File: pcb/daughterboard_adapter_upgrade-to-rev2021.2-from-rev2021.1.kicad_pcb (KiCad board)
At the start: 2 copper layers, 20.2 x 52.2 mm, 4 parts, among them U1 MiniF4, U2 SN74LVC1T45DBV, U3 MiniF4

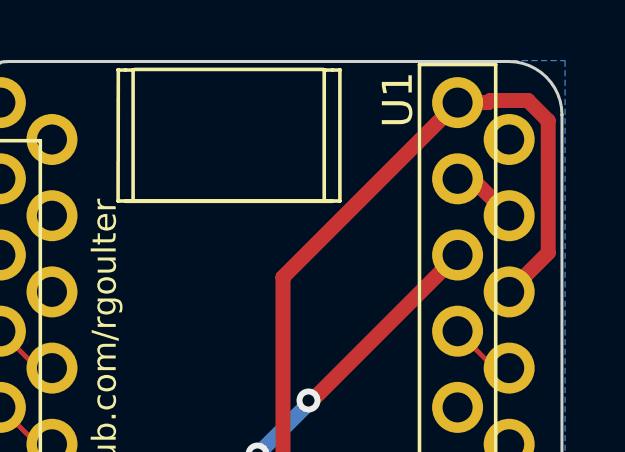
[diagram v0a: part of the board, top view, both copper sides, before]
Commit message: Kicad: Use "5V", "GND", "3V3" in symbol and footprint; update Sch+PCBs
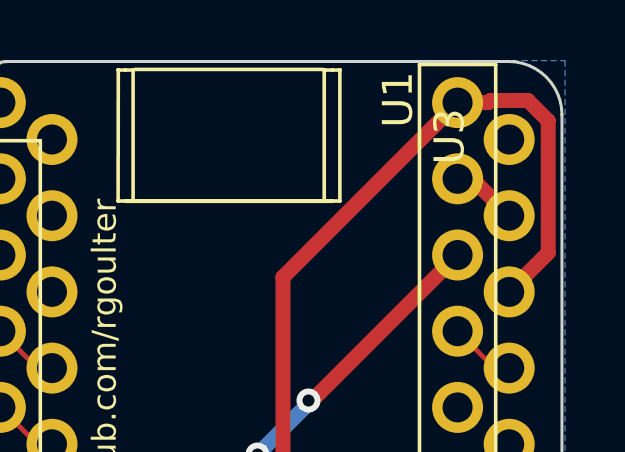
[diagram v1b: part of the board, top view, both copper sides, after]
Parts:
- U1, U3: footprint ProjectLocal:WeAct_MiniF4 -> ProjectLocal:WeAct_MiniF4_Staggerable_rev2020.1

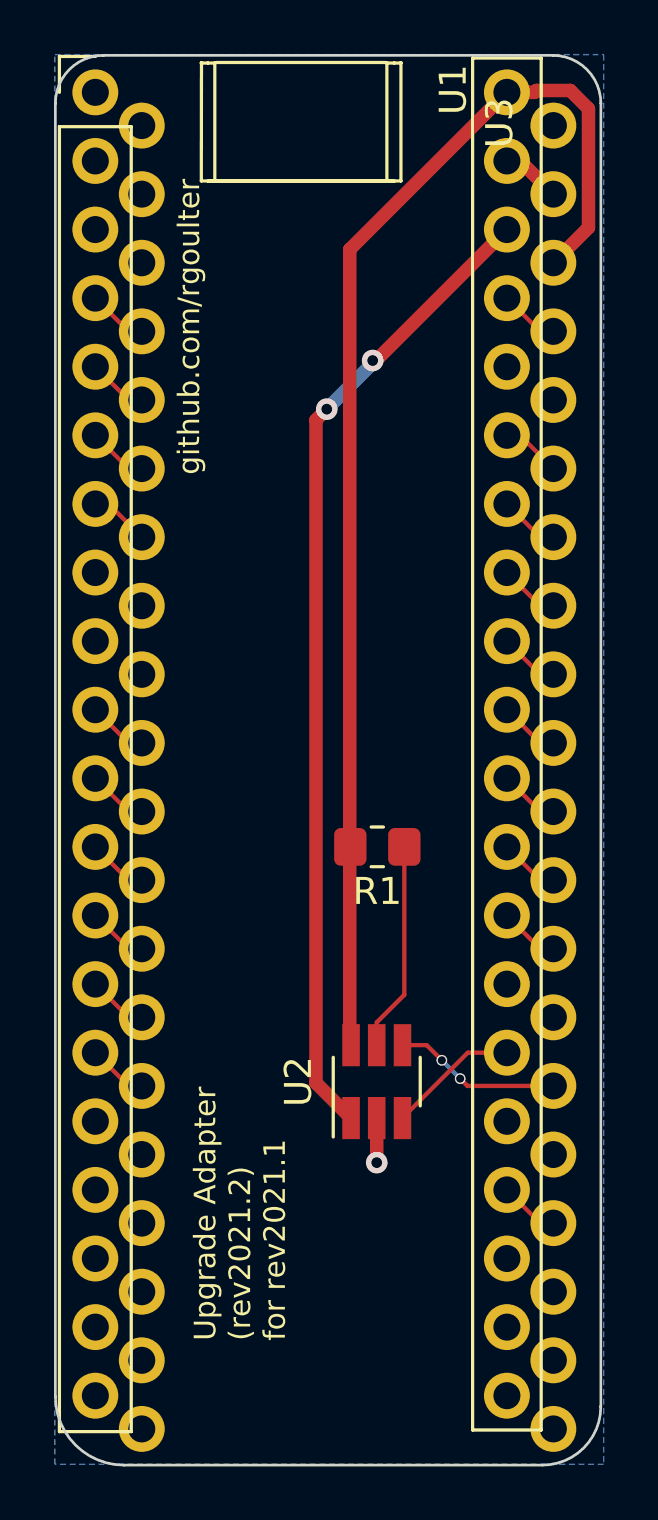
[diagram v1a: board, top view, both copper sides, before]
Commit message: Kicad: plot daughterboards
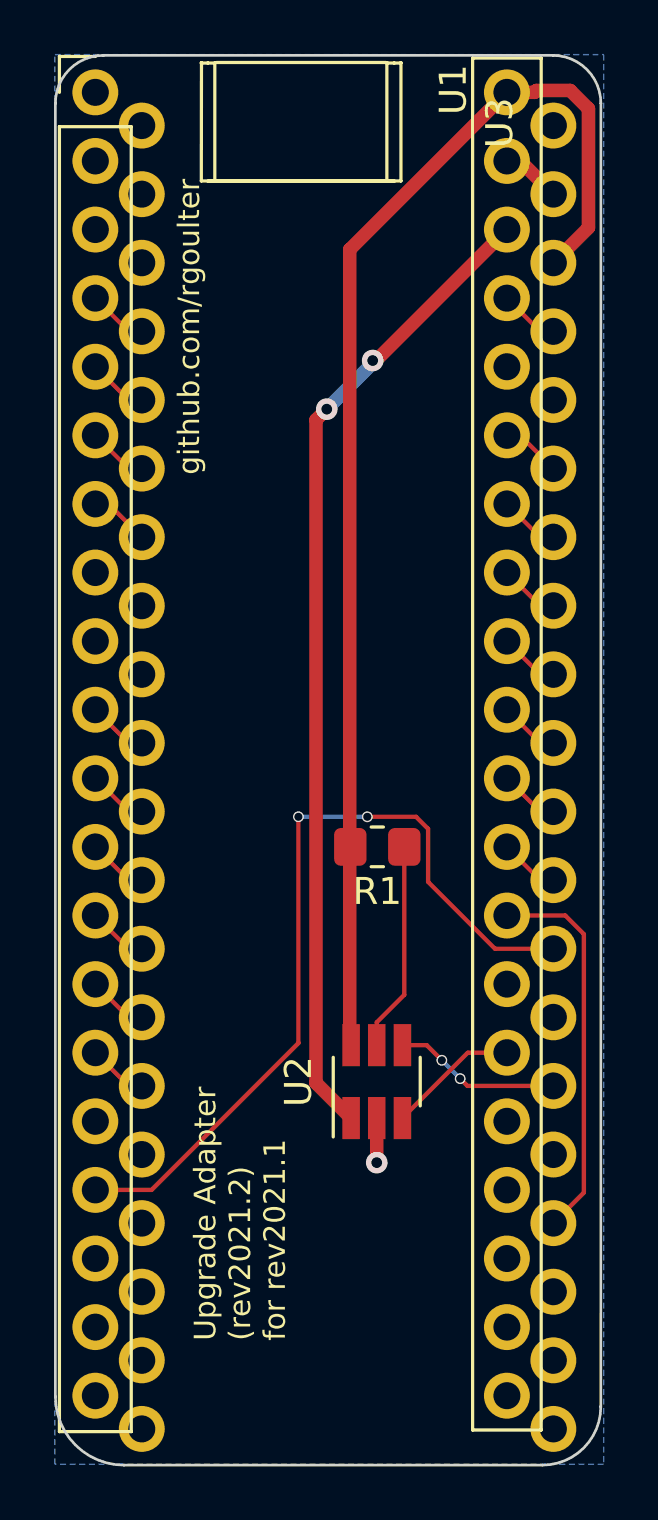
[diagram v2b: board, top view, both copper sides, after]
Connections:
- U1 pad 12: /SW31 -> /SW15
- U1 pad 4: /SW15 -> (no net)
- U1 pad 46: (no net) -> /SW31
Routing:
- net /SW31: track 2.23 -> 31.3 mm, vias 0 -> 2
- net /SW15: track 2.23 -> 14.8 mm
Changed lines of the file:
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@@
     (thickness 1.6)
     (drawings 14)
-    (tracks 74)
+    (tracks 87)
     (zones 0)
     (modules 4)
@@
       (outputformat 1)
       (mirror false)
-      (drillshape 1)
+      (drillshape 0)
       (scaleselection 1)
-      (outputdirectory ""))
+      (outputdirectory "gerber/daughterboard_adapter_for-rev2021.1/"))
   )
   (net 0 "")
@@
       (net 23 /SW24))
     (pad 12 thru_hole circle (at 15.24 30.48) (size 1.7 1.7) (drill 1) (layers *.Cu *.Mask)
-      (net 8 /SW31))
+      (net 15 /SW15))
     (pad 41 thru_hole circle (at 0 30.48) (size 1.7 1.7) (drill 1) (layers *.Cu *.Mask)
       (net 17 /SW21))
@@
     (pad 7 thru_hole circle (at 15.24 38.1) (size 1.7 1.7) (drill 1) (layers *.Cu *.Mask))
     (pad 45 thru_hole circle (at 0 38.1) (size 1.7 1.7) (drill 1) (layers *.Cu *.Mask))
-    (pad 4 thru_hole circle (at 15.24 40.64) (size 1.7 1.7) (drill 1) (layers *.Cu *.Mask)
-      (net 15 /SW15))
-    (pad 46 thru_hole circle (at 0 40.64) (size 1.7 1.7) (drill 1) (layers *.Cu *.Mask))
+    (pad 4 thru_hole circle (at 15.24 40.64) (size 1.7 1.7) (drill 1) (layers *.Cu *.Mask))
+    (pad 46 thru_hole circle (at 0 40.64) (size 1.7 1.7) (drill 1) (layers *.Cu *.Mask)
+      (net 8 /SW31))
     (pad 3 thru_hole circle (at 15.24 43.18) (size 1.7 1.7) (drill 1) (layers *.Cu *.Mask))
     (pad NC_5V thru_hole circle (at 0 43.18) (size 1.7 1.7) (drill 1) (layers *.Cu *.Mask))
@@
       (effects (font (size 0.5 0.5) (thickness 0.08)))
     )
-    (pad 2 smd roundrect (at 1 0 180) (size 1.2 1.4) (layers F.Cu F.Paste F.Mask) (roundrect_rratio 0.208333)
+    (pad 2 smd roundrect (at 1 0 180) (size 1.2 1.4) (layers F.Cu F.Paste F.Mask) (roundrect_rratio 0.2083325)
       (net 1 /5V))
-    (pad 1 smd roundrect (at -1 0 180) (size 1.2 1.4) (layers F.Cu F.Paste F.Mask) (roundrect_rratio 0.208333)
+    (pad 1 smd roundrect (at -1 0 180) (size 1.2 1.4) (layers F.Cu F.Paste F.Mask) (roundrect_rratio 0.2083325)
       (net 26 "Net-(R1-Pad1)"))
     (model ${KISYS3DMOD}/Resistor_SMD.3dshapes/R_0805_2012Metric.wrl
@@
   (segment (start 27.71 35.22) (end 28.2 35.22) (width 0.16) (layer F.Cu) (net 7) (status 30))
   (segment (start 26.48 33.99) (end 27.71 35.22) (width 0.16) (layer F.Cu) (net 7) (status 30))
-  (segment (start 42.95 58.08) (end 43.44 58.08) (width 0.16) (layer F.Cu) (net 8))
-  (segment (start 41.72 56.85) (end 42.95 58.08) (width 0.16) (layer F.Cu) (net 8))
+  (segment (start 42.95 58.08) (end 43.44 58.08) (width 0.16) (layer F.Cu) (net 8) (status 30))
+  (via (at 36.55 53.194) (size 0.4) (drill 0.3) (layers F.Cu B.Cu) (net 8))
+  (segment (start 38.80101 53.63846) (end 38.35655 53.194) (width 0.16) (layer F.Cu) (net 8))
+  (segment (start 38.35655 53.194) (end 36.55 53.194) (width 0.16) (layer F.Cu) (net 8))
+  (segment (start 41.277598 58.08) (end 38.80101 55.603412) (width 0.16) (layer F.Cu) (net 8))
+  (segment (start 38.80101 55.603412) (end 38.80101 53.63846) (width 0.16) (layer F.Cu) (net 8))
+  (segment (start 43.44 58.08) (end 41.277598 58.08) (width 0.16) (layer F.Cu) (net 8))
+  (via (at 34.000001 53.194) (size 0.4) (drill 0.3) (layers F.Cu B.Cu) (net 8))
+  (segment (start 36.55 53.194) (end 34.000001 53.194) (width 0.16) (layer B.Cu) (net 8))
+  (segment (start 28.562402 67.01) (end 26.48 67.01) (width 0.16) (layer F.Cu) (net 8))
+  (segment (start 34.000001 61.572401) (end 28.562402 67.01) (width 0.16) (layer F.Cu) (net 8))
+  (segment (start 34.000001 53.194) (end 34.000001 61.572401) (width 0.16) (layer F.Cu) (net 8))
   (segment (start 27.71 37.76) (end 28.2 37.76) (width 0.16) (layer F.Cu) (net 9) (status 30))
   (segment (start 26.48 36.53) (end 27.71 37.76) (width 0.16) (layer F.Cu) (net 9) (status 30))
@@
   (segment (start 42.95 45.38) (end 43.44 45.38) (width 0.16) (layer F.Cu) (net 14) (status 30))
   (segment (start 41.72 44.15) (end 42.95 45.38) (width 0.16) (layer F.Cu) (net 14) (status 30))
-  (segment (start 42.95 68.24) (end 43.44 68.24) (width 0.16) (layer F.Cu) (net 15))
-  (segment (start 41.72 67.01) (end 42.95 68.24) (width 0.16) (layer F.Cu) (net 15))
+  (segment (start 42.95 68.24) (end 43.44 68.24) (width 0.16) (layer F.Cu) (net 15) (status 30))
+  (segment (start 44.570001 57.537599) (end 44.570001 67.109999) (width 0.16) (layer F.Cu) (net 15))
+  (segment (start 43.882402 56.85) (end 44.570001 57.537599) (width 0.16) (layer F.Cu) (net 15))
+  (segment (start 44.570001 67.109999) (end 43.44 68.24) (width 0.16) (layer F.Cu) (net 15))
+  (segment (start 41.72 56.85) (end 43.882402 56.85) (width 0.16) (layer F.Cu) (net 15))
   (segment (start 42.95 47.92) (end 43.44 47.92) (width 0.16) (layer F.Cu) (net 16) (status 30))
   (segment (start 41.72 46.69) (end 42.95 47.92) (width 0.16) (layer F.Cu) (net 16) (status 30))
-  (segment (start 27.71 58.08) (end 28.2 58.08) (width 0.16) (layer F.Cu) (net 17))
-  (segment (start 26.48 56.85) (end 27.71 58.08) (width 0.16) (layer F.Cu) (net 17))
+  (segment (start 27.71 58.08) (end 28.2 58.08) (width 0.16) (layer F.Cu) (net 17) (status 30))
+  (segment (start 26.48 56.85) (end 27.71 58.08) (width 0.16) (layer F.Cu) (net 17) (status 30))
   (segment (start 42.95 50.46) (end 43.44 50.46) (width 0.16) (layer F.Cu) (net 18) (status 30))
   (segment (start 41.72 49.23) (end 42.95 50.46) (width 0.16) (layer F.Cu) (net 18) (status 30))
